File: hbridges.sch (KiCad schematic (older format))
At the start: 13 parts

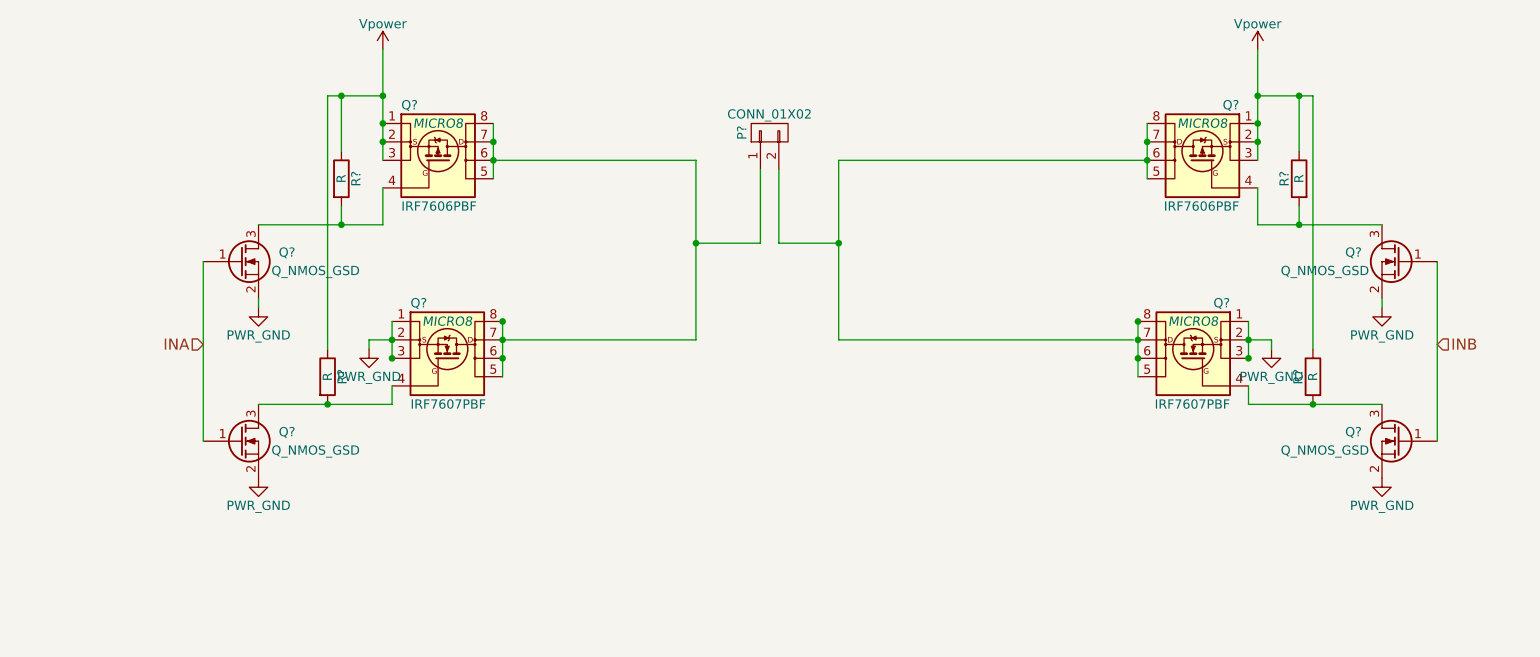
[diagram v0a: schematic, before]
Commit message: added 3 more h-bridges, and routed a bit
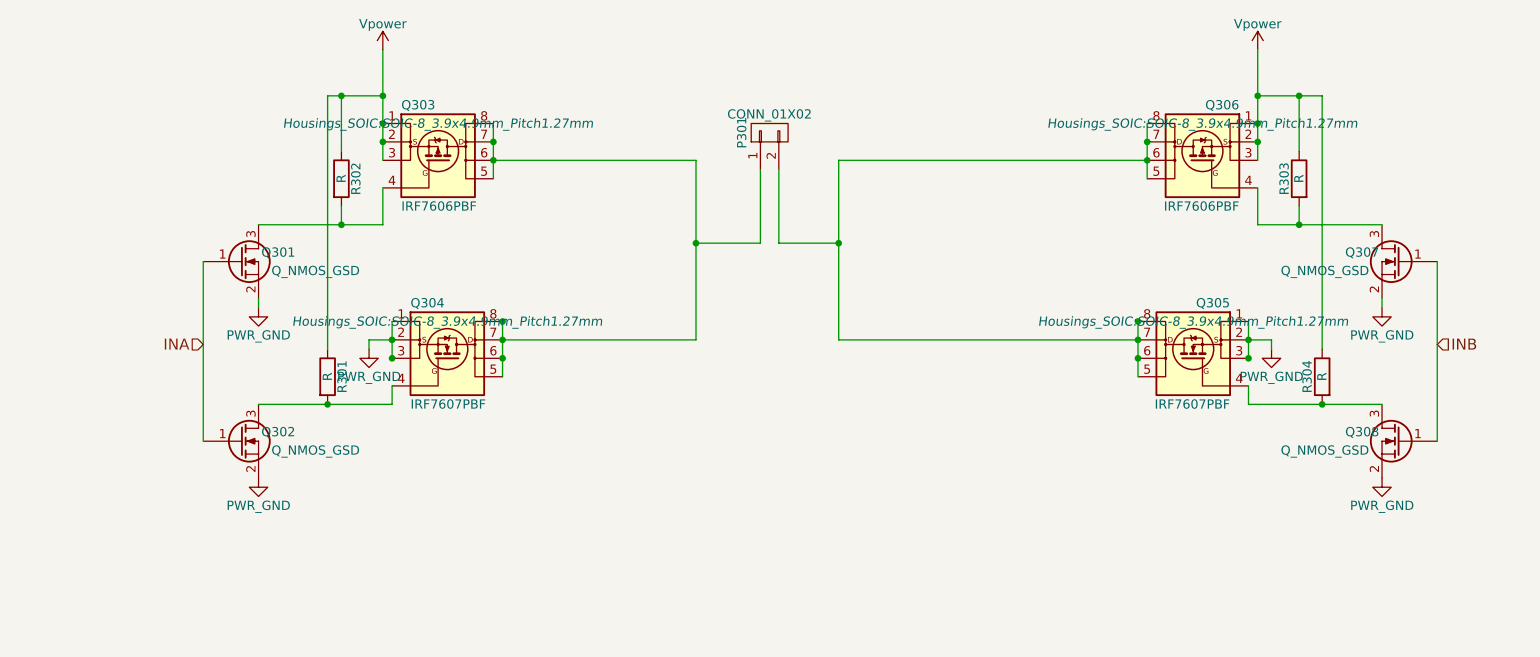
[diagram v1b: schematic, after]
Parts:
- P301: renamed from P?; footprint (none) -> Pin_Headers:Pin_Header_Angled_1x02
- Q301, Q302: renamed from Q?; footprint (none) -> TO_SOT_Packages_SMD:SOT-23_Handsoldering
- Q303, Q304, Q305, Q306: renamed from Q?; footprint MICRO8 -> Housings_SOIC:SOIC-8_3.9x4.9mm_Pitch1.27mm
- Q307, Q308: renamed from Q?; footprint (none) -> TO_SOT_Packages_SMD:SOT-23
- R301, R302, R303, R304: renamed from R?; footprint (none) -> Resistors_SMD:R_0805_HandSoldering
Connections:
- net at Q305.5 (D), Q305.6 (D), Q305.7 (D)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: now also P301.2 (P2), Q306.5 (D), Q306.6 (D), Q306.7 (D), Q306.8 (D)
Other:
- moved on the sheet: R304

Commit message: Added requirements
Also selected components for certain things.
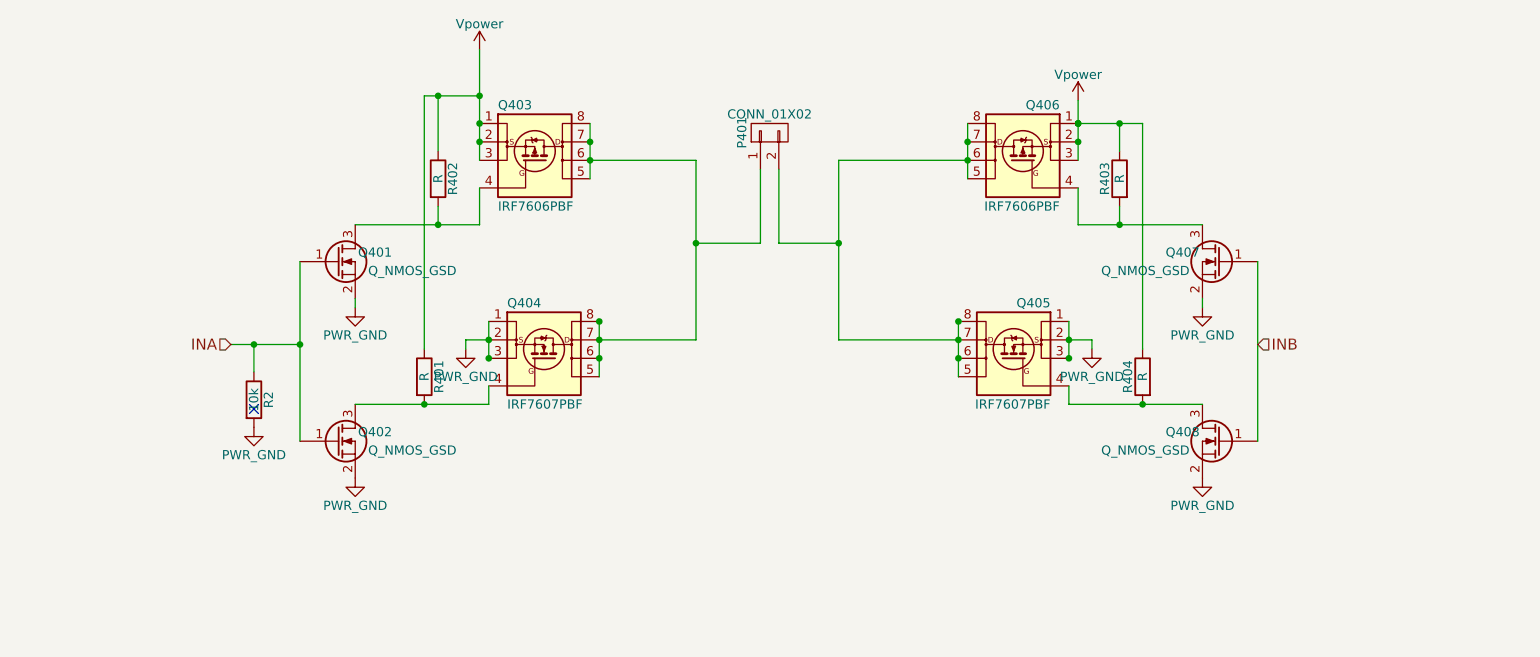
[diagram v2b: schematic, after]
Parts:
- added R1: 10k, Resistors_SMD:R_0805_HandSoldering, symbol R
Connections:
- net INA: now also R1.1
- net PWR_GND: now also R1.2
- no-connect marks 0 -> 1
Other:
- moved on the sheet: Q401, Q402, Q403, Q404, Q405, Q406, Q407, Q408, R401, R402, R403, R404

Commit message: Routed a h-bridge. Damn that's a lot of work.
also assigned a lot of components.
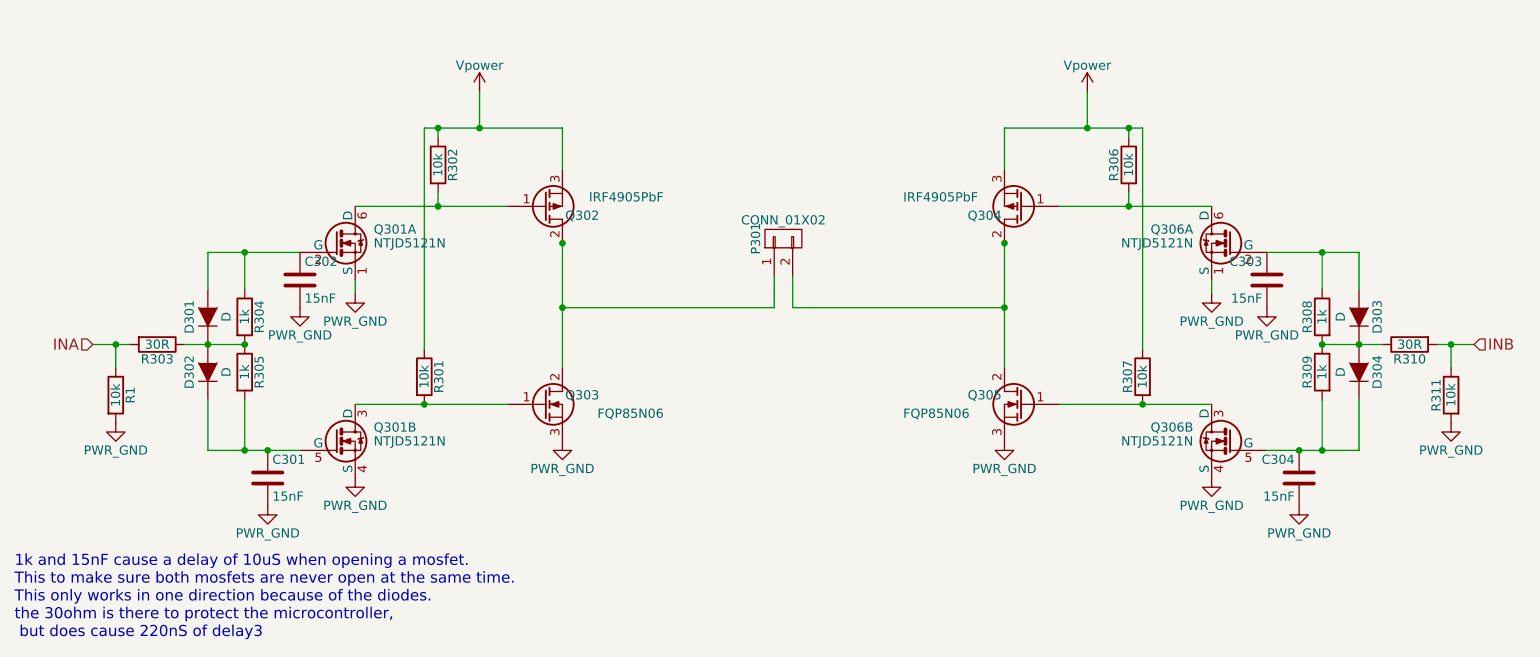
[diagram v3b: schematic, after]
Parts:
- removed Q301, Q302: Q_NMOS_GSD, TO_SOT_Packages_SMD:SOT-23_Handsoldering, symbol Q_NMOS_GSD
- removed Q303, Q306: IRF7606PBF, Housings_SOIC:SOIC-8_3.9x4.9mm_Pitch1.27mm, symbol IRF7606PBF
- removed Q304, Q305: IRF7607PBF, Housings_SOIC:SOIC-8_3.9x4.9mm_Pitch1.27mm, symbol IRF7607PBF
- removed Q307, Q308: Q_NMOS_GSD, TO_SOT_Packages_SMD:SOT-23, symbol Q_NMOS_GSD
- removed R303, R304: R, Resistors_SMD:R_0805_HandSoldering, symbol R
- added C601, C602, C603, C604: 15nF, lib:R_0402_handsoldering, symbol C
- added D303, D304, D601, D602: D, Diodes_SMD:SOD-323, symbol D
- added Q304, Q602: IRF4905PbF, Power_Integrations:TO-220, symbol IRF4905PbF
- added Q305, Q603: FQP85N06, Power_Integrations:TO-220, symbol FQP85N06
- added Q306, Q601: NTJD5121N, lib:SOT-363, symbol NTJD5121N
- added R306, R307, R311: 10k, lib:R_0402_handsoldering, symbol R
- added R310, R603: 30R, lib:R_0402_handsoldering, symbol R
- added R604, R605, R608, R609: 1k, lib:R_0402_handsoldering, symbol R
- P301: footprint Pin_Headers:Pin_Header_Angled_1x02 -> Pin_Headers:Pin_Header_Straight_1x02
- R1: footprint Resistors_SMD:R_0805_HandSoldering -> lib:R_0402_handsoldering
- R301, R302: value R -> 10k; footprint Resistors_SMD:R_0805_HandSoldering -> lib:R_0402_handsoldering
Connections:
- net INA: now also R603.2
- net INB: now also R310.2, R311.1
- net PWR_GND: now also C601.2, C602.2, C603.2, C604.2, Q305.3 (S), Q306.1 (S), Q306.4 (S), Q601.1 (S), Q601.4 (S), Q603.3 (S), R311.2
- net Vpower: now also Q304.3 (S), Q602.3 (S), R306.1, R307.1
- net at R301.2: now also Q601.3 (D), Q603.1 (G)
- net at P301.1 (P1): now also Q602.2 (D), Q603.2 (D)
- net at R302.2: now also Q601.6 (D), Q602.1 (G)
- net at P301.2 (P2): now also Q304.2 (D), Q305.2 (D)
- new net: C602.1, D601.2 (A), Q601.2 (G), R604.1
- new net: D601.1 (K), D602.2 (A), R603.1, R604.2, R605.1
- new net: C601.1, D602.1 (K), Q601.5 (G), R605.2
- new net: Q304.1 (G), Q306.6 (D), R306.2
- new net: Q305.1 (G), Q306.3 (D), R307.2
- new net: C603.1, D303.2 (A), Q306.2 (G), R608.1
- new net: D303.1 (K), D304.2 (A), R310.1, R608.2, R609.1
- new net: C604.1, D304.1 (K), Q306.5 (G), R609.2
- no-connect marks 1 -> 0
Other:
- note added: "1k and 15nF cause a delay of 10uS when opening a mosfet.\nThis to make sure both mosfets are never open at the same time. \nThis only works in one direction because of the diodes.\nthe 30ohm is there to protect the microcontroller,\n but does cause 220nS of delay3"
- moved on the sheet: P301, R1, R302
